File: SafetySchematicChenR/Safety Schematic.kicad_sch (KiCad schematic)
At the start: 0 parts

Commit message: rough draft schematic
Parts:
- added C1, C2, C3, C4, C5: C_Small, symbol Device:C_Small
- added D1, D2, D3: LED, symbol Device:LED
- added D4: 1N4148WT, Diode_SMD:D_SOD-523, symbol Diode:1N4148WT
- added J1: XT60-M, SMV_Connectors:AMASS_XT60-M, symbol SMV_Custom:XT60-M
- added J2, J5, J6: 430450200, SMV_Connectors:CONN_SD-43045-001_02_MOL, symbol SMV_Custom:430450200
- added J3: Conn_01x04_Pin, symbol Connector:Conn_01x04_Pin
- added J4: 22035035, SMV_Connectors:3pin_CON_22035035_MOL, symbol SMV_Custom:3-pin Mini Molex Spox
- added K1: Fujitsu_FTR-LYAA005x, Relay_THT:Relay_SPST-NO_Fujitsu_FTR-LYAA005x_FormA_Vertical, symbol Relay:Fujitsu_FTR-LYAA005x
- added Q1: IRLML6344TRPBF, IRLML6344TRPBF:TRANS_IRLML6344TRPBF, symbol SMV_Custom:IRLML6344TRPBF
- added R1, R2, R3, R4, R5, R6, R7: R_Small, symbol Device:R_Small
- added U1: 74LVC2G08, symbol 74xGxx:74LVC2G08
- added U10: MCP2562-E/P, PDIP8_300MC_MCH, symbol SMV_Custom:MCP2562-E_P
- added U11: 74AUC2G32, symbol 74xGxx:74AUC2G32
- added U2: 74LS05, symbol 74xx:74LS05
- added U5: MCP6286T-E/OT, SOT-23-5_MC_MCH, symbol SMV_Custom:MCP6286T-E_OT
- added U7: 74LS279, symbol 74xx:74LS279
- added U8: LM2936-5.0_TO92, Package_TO_SOT_THT:TO-92_Inline, symbol Regulator_Linear:LM2936-5.0_TO92
- added U9: ~, symbol SMV_Custom:STM32_Nucleo_F446RE
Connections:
- new net: Q1.1, R5.1
- new net: D3.1 (K), R5.2
- new net: D2.2 (A), R4.2
- new net: U2.1, U7.4 (Q)
- new net: U1.1, U2.2
- new net: J4.3, U10.6 (CANL)
- new net: J4.1, U10.7 (CANH)
- new net: D3.2 (A), U1.7
- new net: U11.7, U7.2 (~{S})
- new net: D1.2 (A), R2.2
- new net +12V: J6.2
- new net +3V: C3.1, C4.2, D4.1 (K), J2.2, J3.1 (Pin_1), J5.2, K1.A1, Q1.2, U11.2, U5.1 (VOUT), U5.5 (VDD), U8.1 (VO), U9.24 (VIN)
- new net +48V: J1.P (POS), K1.13
- new net CANIN: U10.1 (TXD), U9.50 (PA12)
- new net CANOUT: U10.4 (RXD), U9.52 (PA11)
- new net DRAIN: D4.2 (A), K1.A2, Q1.3
- new net EXTESTOP: J2.1, R2.1, U7.3 (~{S})
- new net GND: C1.1, C2.1, C3.2, C4.1, C5.2, D1.1 (K), D2.1 (K), J1.N (NEG), J3.4 (Pin_4), J4.2, K1.14, R1.2, R3.2, R6.2, R7.2, U10.2 (VSS), U10.8 (STBY), U5.2 (VSS), U8.2 (GND), U9.20 (GND)
- new net HSENSOR: J3.2 (Pin_2), R4.1, U5.3 (VIN+)
- new net IGNITION: R1.1, U1.2, U9.38 (PC0)
- new net INTESTOP: R3.1, U11.1, U9.36 (PC1)
- new net LDOIN: C5.1, J6.1, R7.1, U8.3 (VI)
- new net RESET: J5.1, R6.1, U7.1 (~{R})
- new net SPLIT: C2.2, U10.5 (SPLIT), U9.16 (+3V3)
- new net TRANSPWIN: C1.2, U10.3 (VDD), U9.18 (+5V)
- no-connect marks 0 -> 62
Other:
- note added: "Boost Convertor"

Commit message: feedback updates
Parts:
- removed U1: 74LVC2G08, symbol 74xGxx:74LVC2G08
- removed U11: 74AUC2G32, symbol 74xGxx:74AUC2G32
- removed U2: 74LS05, symbol 74xx:74LS05
- removed U5: MCP6286T-E/OT, SOT-23-5_MC_MCH, symbol SMV_Custom:MCP6286T-E_OT
- removed U8: LM2936-5.0_TO92, Package_TO_SOT_THT:TO-92_Inline, symbol Regulator_Linear:LM2936-5.0_TO92
- added C10, C11, C6, C7, C8, C9: C_Small, symbol Device:C_Small
- added D5: 1N4148WT, Diode_SMD:D_SOD-523, symbol Diode:1N4148WT
- added J7: XT60-M, SMV_Connectors:AMASS_XT60-M, symbol SMV_Custom:XT60-M
- added R10: 120 ohms, symbol Device:R_Small
- added R8: 0.1k ohms, symbol Device:R_Small
- added R9: 100,000k ohms, symbol Device:R_Small
- added U1: 74AHC1G32, symbol 74xGxx:74AHC1G32
- added U11: 74AHC1G08, symbol 74xGxx:74AHC1G08
- added U12: MCP6286T-E/OT, SOT-23-5_MC_MCH, symbol SMV_Custom:MCP6286T-E_OT
- added U13, U4: MAX603, symbol Regulator_Linear:MAX603
- added U2, U5, U8: 74LVC1GU04DRL, Package_TO_SOT_SMD:SOT-553, symbol 74xGxx:74LVC1GU04DRL
- added U3: LT1962-3, Package_SO:MSOP-8_3x3mm_P0.65mm, symbol Regulator_Linear:LT1962-3
- added U6: Inverter_Schmitt_Dual, symbol 74xGxx:Inverter_Schmitt_Dual
- R1, R3, R4: value R_Small -> 5k ohms
- R2, R6: value R_Small -> 10k ohms
- R7: value R_Small -> 12 ohms
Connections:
- net TRANSPWIN is gone; now on net +5V: C1.2, U10.3 (VDD), U9.18 (+5V)
- net +12V: now also J6.1, Q1.2, C9.1, D5.1 (K), U4.1 (IN), U4.4 (~{OFF}); no longer J6.2
- net +48V: now also J7.P (POS); no longer J1.P (POS), K1.13
- net DRAIN: now also D5.2 (A)
- net EXTESTOP: now also D2.2 (A), R2.2; no longer J2.1, R2.1, U7.3 (~{S})
- net GND: now also C4.2, C5.1, J6.2, R7.1, U9.19 (GND), U9.22 (GND), U9.47 (GND), U9.58 (GND), U9.8 (GND), C10.2, C11.2, C6.2, C7.2, C8.1, C9.2, R8.1, R9.2, U1.3 (GND), U11.3 (GND), U12.1 (VOUT), U12.2 (VSS), U13.1 (IN), U13.2 (GND), U13.3 (GND), U13.4 (~{OFF}), U13.5 (SET), U13.6 (GND), U13.7 (GND), U2.3 (GND), U3.2 (SENSE), U3.4 (GND), U4.2 (GND), U4.3 (GND), U4.5 (SET), U4.6 (GND), U4.7 (GND), U5.3 (GND), U6.2 (GND), U8.3 (GND); no longer C4.1, D1.1 (K), D2.1 (K), K1.14, R1.2, R3.2, R6.2, R7.2
- net HSENSOR: now also R4.2, U12.3 (VIN+); no longer J3.2 (Pin_2), R4.1
- net IGNITION: now also R1.2, U11.1; no longer R1.1, U9.38 (PC0)
- net INTESTOP: now also D1.2 (A); no longer U9.36 (PC1)
- net RESET: now also R6.2, U5.2; no longer J5.1, R6.1, U7.1 (~{R})
- net SPLIT: no longer U9.16 (+3V3)
- net +5V: now reaches U9.6 (E5V)
- net +5V: now also C4.1, J2.2, J5.2, C10.1, C6.1, U1.5 (VCC), U11.5 (VCC), U12.5 (VDD), U2.5 (VCC), U3.5 (~{SHDN}), U3.8 (IN), U4.8 (OUT), U5.5 (VCC), U6.5 (V_{CC}), U8.5 (VCC)
- net at U7.4 (Q): now also U8.2
- net at J4.3, U10.6 (CANL): now also R10.1
- net at J4.1, U10.7 (CANH): now also R10.2
- net at D3.2 (A): now also U11.4
- net at U7.2 (~{S}): now also U1.4
- removed net +3V: C3.1, C4.2, D4.1 (K), J2.2, J3.1 (Pin_1), J5.2, K1.A1, Q1.2, U9.24 (VIN)
- removed net LDOIN: C5.1, J6.1, R7.1
- new net: U5.4, U7.1 (~{R})
- new net: R1.1, U9.38 (PC0)
- new net: R8.2, R9.1, U12.4 (VIN-)
- new net: J3.2 (Pin_2), R4.1
- new net: R3.2, U9.36 (PC1)
- new net: D4.1 (K), K1.A1
- new net: J1.P (POS), K1.13
- new net: U11.2, U8.4
- new net: J5.1, R6.1
- new net: D2.1 (K), U6.1 (1A)
- new net: D1.1 (K), U6.3 (2A)
- new net: U1.1, U6.4 (2Y)
- new net: U1.2, U6.6 (1Y)
- new net: U2.4, U7.3 (~{S})
- new net: C7.1, U3.3 (BYP)
- new net: J2.1, R2.1
- new net: J7.N (NEG), K1.14
- new net +3V0: C3.1, C8.2, J3.1 (Pin_1), R7.2, U3.1 (OUT)
- new net +3V3: U9.16 (+3V3)
- new net OPAMPLDO: C11.1, U13.8 (OUT), U2.2
- no-connect marks 62 -> 57
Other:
- moved on the sheet: D2, D3, D4, J1, J4, K1, Q1, R3, R4, R5

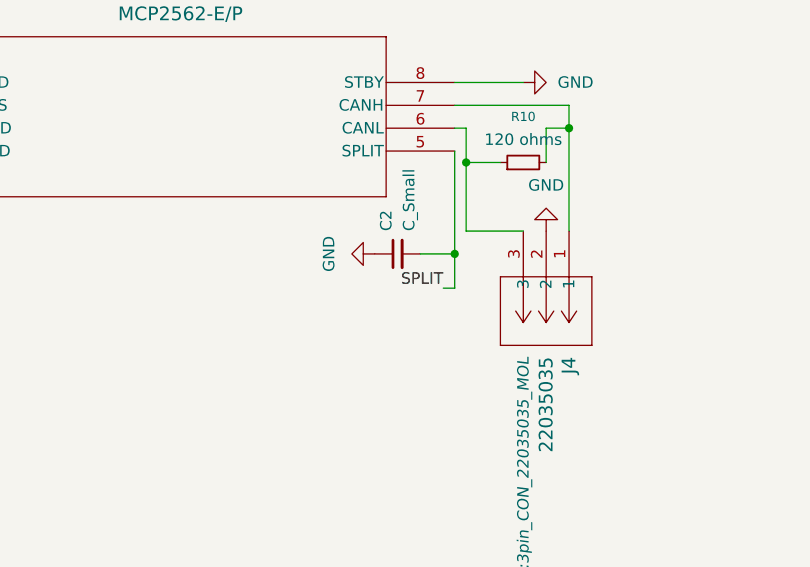
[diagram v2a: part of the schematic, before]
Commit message: changed SPLIT pin to 5V
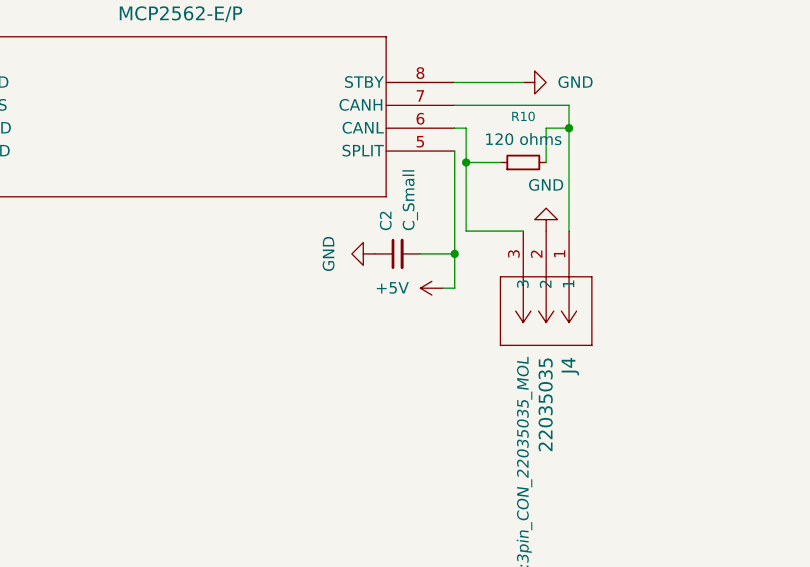
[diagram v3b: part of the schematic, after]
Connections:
- net SPLIT is gone; now on net +5V: C2.2, U10.5 (SPLIT)
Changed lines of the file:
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@@
 		)
 	)
-	(label "SPLIT"
-		(at 158.75 196.85 180)
-		(effects
-			(font
-				(size 1.27 1.27)
-			)
-			(justify right bottom)
-		)
-	)
 	(label "EXTESTOP"
 		(at 81.28 128.27 90)
@@
 					(unit 1)
 				)
+			)
+		)
+	)
+	(symbol
+		(lib_id "power:+5V")
+		(at 158.75 196.85 90)
+		(unit 1)
+		(exclude_from_sim no)
+		(in_bom yes)
+		(on_board yes)
+		(dnp no)
+		(fields_autoplaced yes)
+		(property "Reference" "#PWR054"
+			(at 162.56 196.85 0)
+			(effects
+				(font
+					(size 1.27 1.27)
+				)
+				(hide yes)
+			)
+		)
+		(property "Value" "+5V"
+			(at 154.94 196.8499 90)
+			(effects
+				(font
+					(size 1.27 1.27)
+				)
+				(justify left)
+			)
+		)
+		(property "Footprint" ""
+			(at 158.75 196.85 0)
+			(effects
+				(font
+					(size 1.27 1.27)
+				)
+				(hide yes)
+			)
+		)
+		(property "Datasheet" ""
+			(at 158.75 196.85 0)
+			(effects
+				(font
+					(size 1.27 1.27)
+				)
+				(hide yes)
+			)
+		)
+		(property "Description" "Power symbol creates a global label with name \"+5V\""
+			(at 158.75 196.85 0)
+			(effects
+				(font
+					(size 1.27 1.27)
+				)
+				(hide yes)
+			)
+		)
+		(pin "1"
+		)
+		(instances
+			(project ""
+				(path "/927e5849-97d5-445f-9a77-6290d281bda7"
+					(reference "#PWR054")
+					(unit 1)
+				)

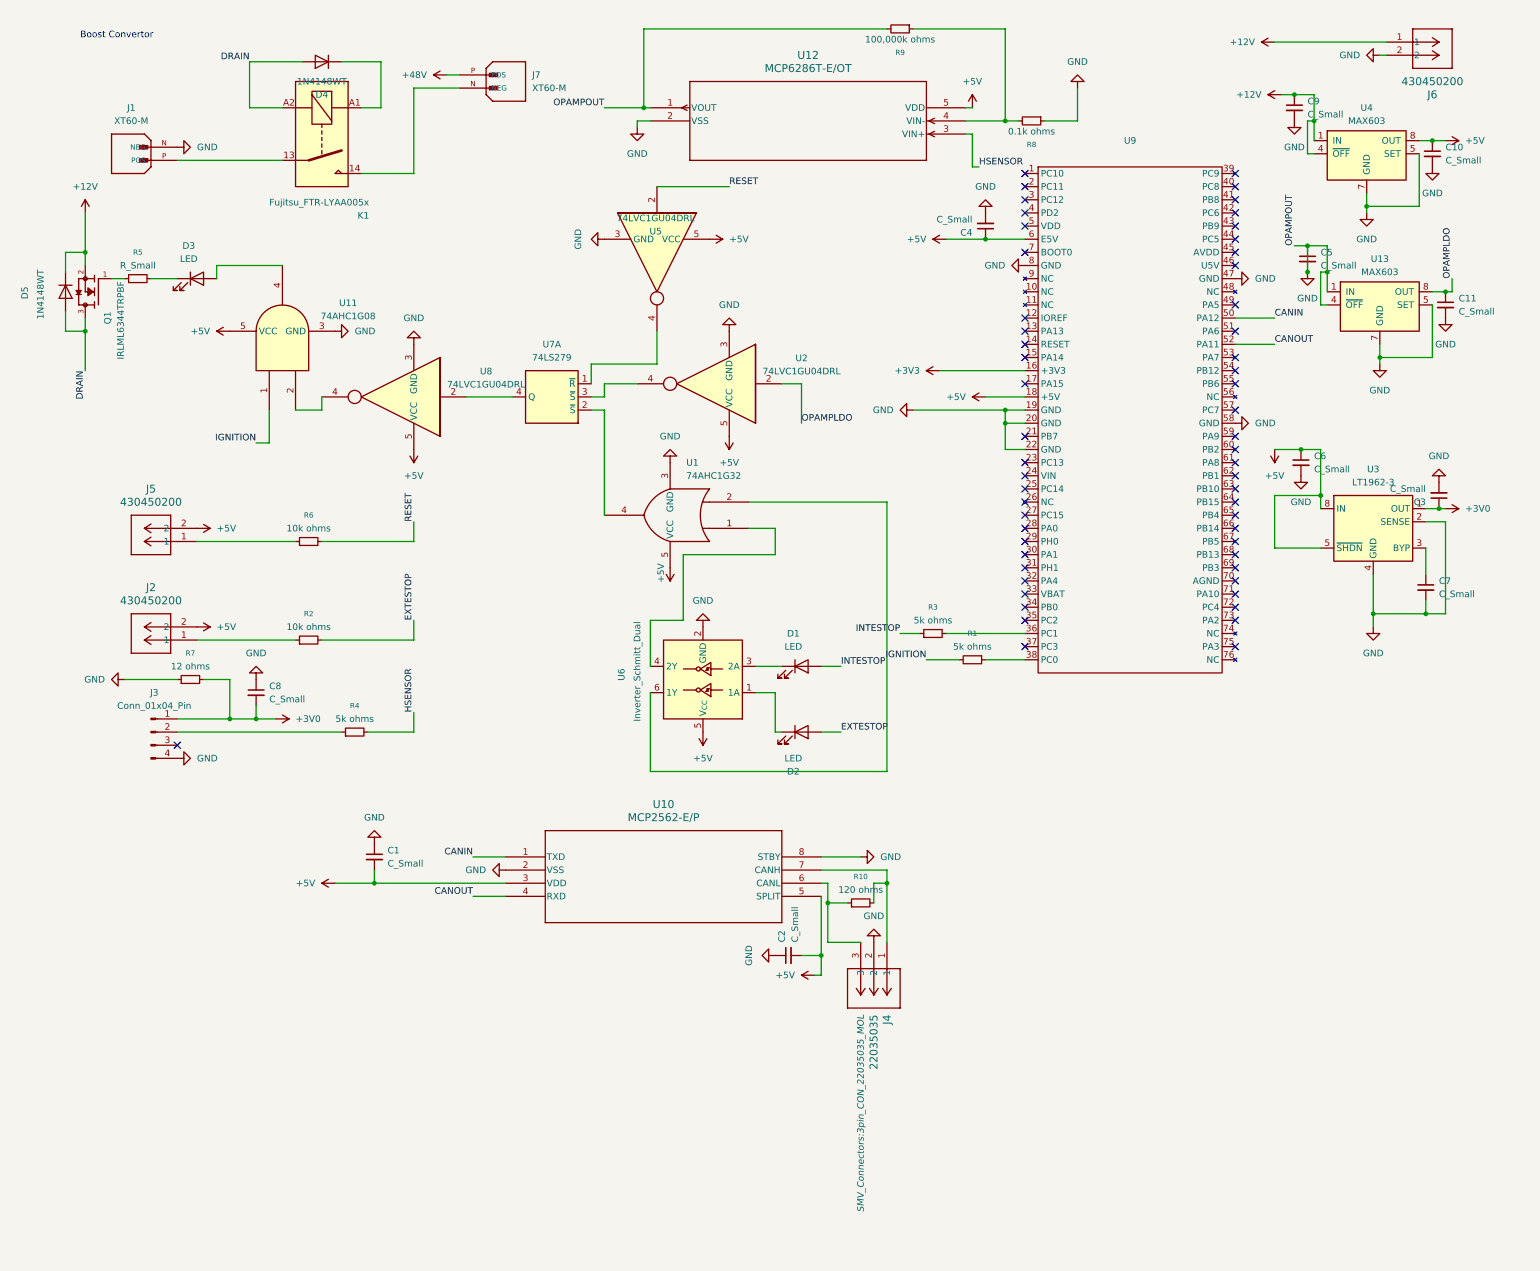
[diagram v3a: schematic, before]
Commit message: added capacitor values
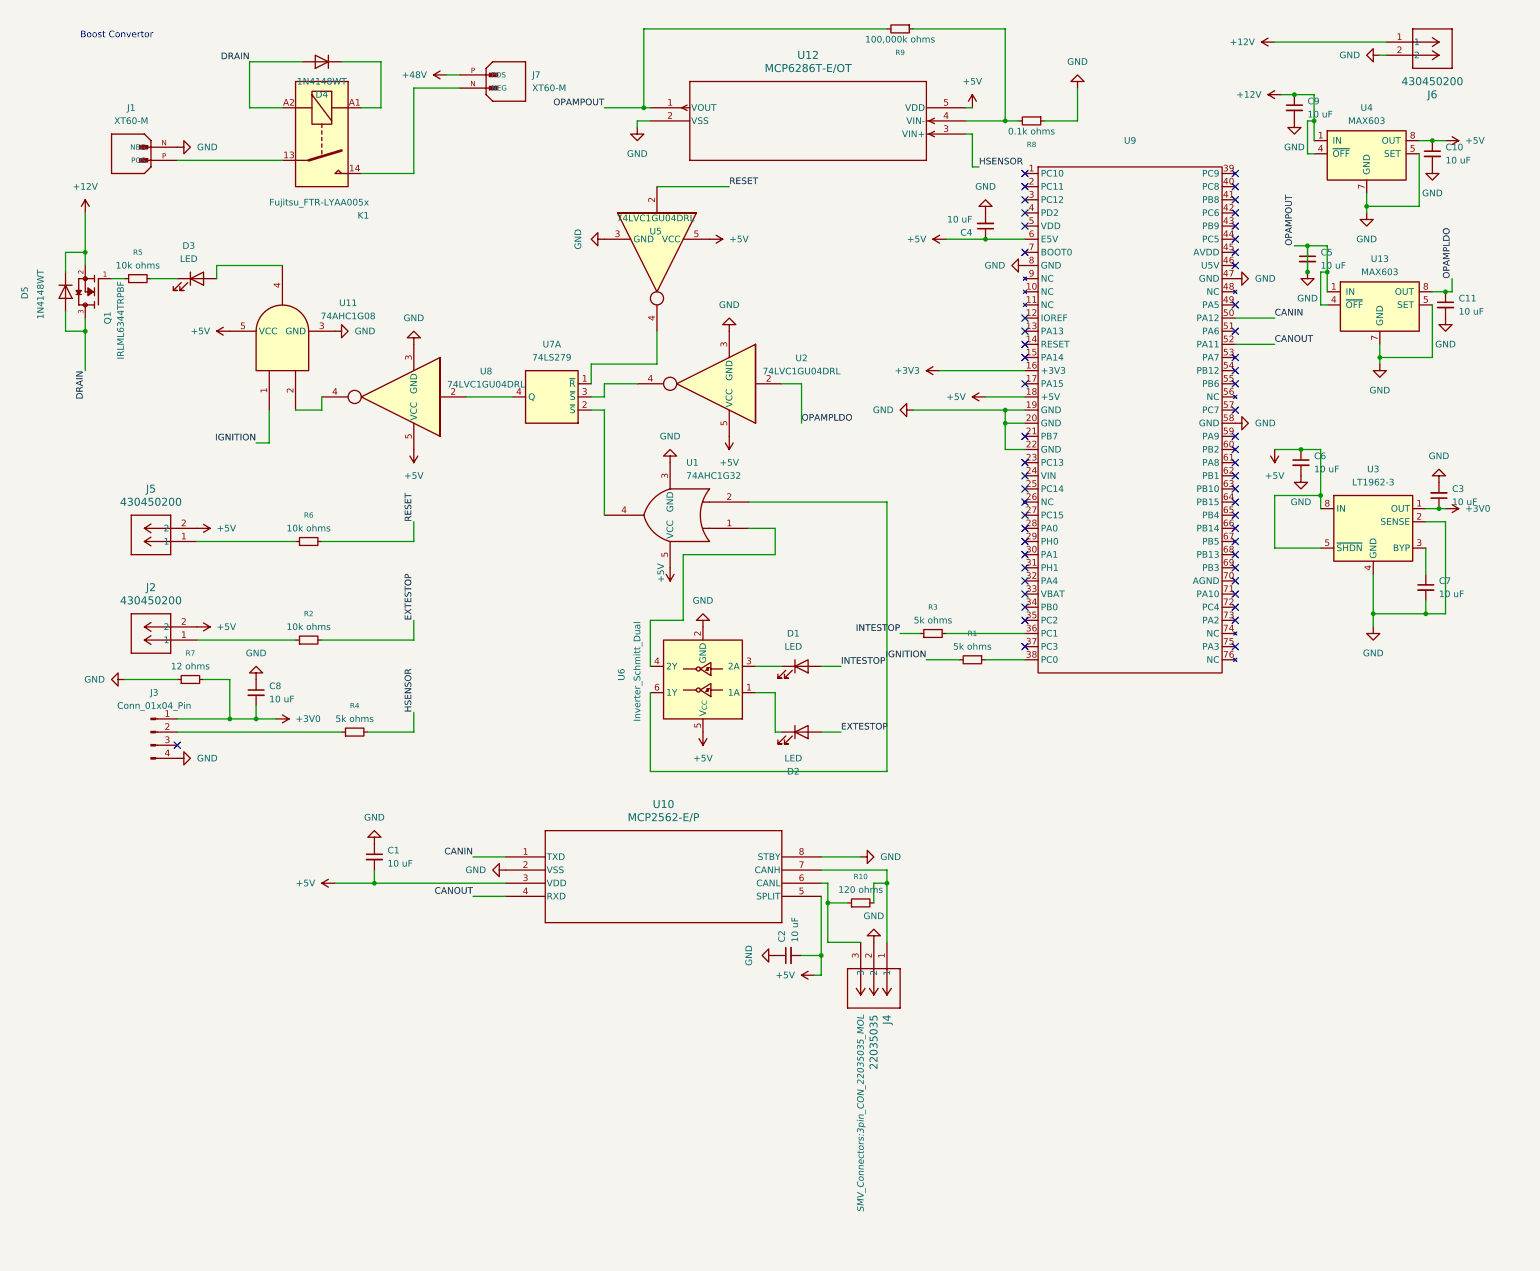
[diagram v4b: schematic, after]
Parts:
- C1, C10, C11, C2, C3, C4, C5, C6, C7, C8, C9: value C_Small -> 10 uF
- R5: value R_Small -> 10k ohms
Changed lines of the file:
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@@
 			)
 		)
-		(property "Value" "R_Small"
+		(property "Value" "10k ohms"
 			(at 27.94 59.69 90)
 			(effects
@@
 			)
 		)
-		(property "Value" "C_Small"
+		(property "Value" "10 uF"
 			(at 76.2 175.2662 0)
 			(effects
@@
 			)
 		)
-		(property "Value" "C_Small"
+		(property "Value" "10 uF"
 			(at 53.34 143.5162 0)
 			(effects
@@
 		(fields_autoplaced yes)
 		(property "Reference" "C3"
-			(at 276.86 105.4038 0)
+			(at 281.94 102.8635 0)
 			(effects
 				(font
 					(size 1.27 1.27)
 				)
-				(justify left)
+				(justify right)
 			)
 		)
-		(property "Value" "C_Small"
-			(at 276.86 102.8638 0)
+		(property "Value" "10 uF"
+			(at 281.94 105.4035 0)
 			(effects
 				(font
 					(size 1.27 1.27)
 				)
-				(justify left)
+				(justify right)
 			)
 		)
@@
 			)
 		)
-		(property "Value" "C_Small"
+		(property "Value" "10 uF"
 			(at 254 30.4862 0)
 			(effects
@@
 			)
 		)
-		(property "Value" "C_Small"
+		(property "Value" "10 uF"
 			(at 154.9462 190.5 0)
 			(effects
@@
 			)
 		)
-		(property "Value" "C_Small"
+		(property "Value" "10 uF"
 			(at 280.67 39.3762 0)
 			(effects
@@
 			)
 		)
-		(property "Value" "C_Small"
+		(property "Value" "10 uF"
 			(at 256.54 59.6962 0)
 			(effects
@@
 			)
 		)
-		(property "Value" "C_Small"
+		(property "Value" "10 uF"
 			(at 279.4 123.1962 0)
 			(effects
@@
 			)
 		)
-		(property "Value" "C_Small"
+		(property "Value" "10 uF"
 			(at 255.27 99.0662 0)
 			(effects
@@
 		(on_board yes)
 		(dnp no)
-		(fields_autoplaced yes)
 		(property "Reference" "C4"
 			(at 189.23 53.3338 0)
@@
 			)
 		)
-		(property "Value" "C_Small"
+		(property "Value" "10 uF"
 			(at 189.23 50.7938 0)
 			(effects
@@
 			)
 		)
-		(property "Value" "C_Small"
+		(property "Value" "10 uF"
 			(at 283.21 68.5862 0)
 			(effects
